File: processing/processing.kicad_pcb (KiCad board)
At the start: 2 copper layers, 26 parts, among them J1 HRO-TYPE-C-31-M-12, J2 Conn_01x03, J3 ICSP, SW1 SW_RESET, U1 CH340G, U2 ATmega328P-AU, Y1 12MHz, Y2 16MHz

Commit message: base audio board
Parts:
- R3, R4: footprint Resistor_SMD:R_1206_3216Metric -> Resistor_SMD:R_0603_1608Metric
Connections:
- J1 pad B4: Net-(F1-Pad2) -> (no net)
- J1 pad B9: Net-(F1-Pad2) -> (no net)

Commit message: finish the processing board
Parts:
- added J3: Conn_01x05, Connector_PinSocket_2.54mm:PinSocket_1x05_P2.54mm_Vertical, F.Cu at (155.4, 76.5)
- added J4: HRO-TYPE-C-31-M-12, Connector_USB:USB_C_Receptacle_HRO_TYPE-C-31-M-12, F.Cu at (150.3, 119.5)
- J1: value HRO-TYPE-C-31-M-12 -> Conn_01x02; footprint Connector_USB:USB_C_Receptacle_HRO_TYPE-C-31-M-12 -> Connector_PinSocket_2.54mm:PinSocket_1x02_P2.54mm_Vertical
- J2: footprint Connector_PinHeader_2.54mm:PinHeader_1x03_P2.54mm_Vertical -> Connector_PinSocket_2.54mm:PinSocket_1x03_P2.54mm_Vertical
- moved C10 32.1 mm to (137.3, 96.0), turned to 270 degrees
- moved J1 30.6 mm to (130.3, 97.8), turned to 180 degrees
- moved C9 29.7 mm to (137.8, 93.5)
- moved C8 29.4 mm to (140.8, 93.5), turned to 180 degrees
- moved L1 28.4 mm to (153.1, 106.5), turned to 270 degrees
- moved C4 28.2 mm to (164.1, 101.2), turned to 180 degrees
- moved Y2 26.2 mm to (140.3, 96.3), turned to 180 degrees
- moved R5 26.0 mm to (143.3, 96.5)
- moved U2 25.2 mm to (150.3, 96.5), turned to 315 degrees
- moved C6 23.8 mm to (155.1, 106.7), turned to 270 degrees
- moved U1 21.4 mm to (164.1, 107.3), turned to 0 degrees
- moved C7 21.2 mm to (153.2, 103.8)
- moved J5 20.1 mm to (138.8, 110.8), turned to 180 degrees
- moved SW1 19.7 mm to (162.1, 83.8), turned to 180 degrees
- moved C2 18.6 mm to (157.8, 107.4)
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- renumbered J3 to J5
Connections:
- J2 pad 3: A3 -> A2
- R1 pad 1: Net-(J1-PadA5) -> Net-(J4-PadA5)
- R2 pad 2: Net-(J1-PadB5) -> Net-(J4-PadB5)
- U1 pad 5: Net-(J1-PadA6) -> Net-(J4-PadA6)
- U1 pad 6: Net-(J1-PadA7) -> Net-(J4-PadA7)
- U2 pad 1: Net-(U2-Pad1) -> D2
- U2 pad 10: Net-(U2-Pad10) -> D5
- U2 pad 2: Net-(U2-Pad2) -> D3
- U2 pad 32: Net-(U2-Pad32) -> D1
- U2 pad 9: Net-(U2-Pad9) -> D4
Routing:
- net +5V: track 17.5 -> 106.7 mm, vias 0 -> 8
- net RESET: track 0.00 -> 43.4 mm, vias 0 -> 3
- net GND: track 44.9 -> 77.7 mm, vias 10 -> 9
- net D5: track 0.00 -> 26.4 mm, vias 0 -> 2
- net D4: track 0.00 -> 25.1 mm, vias 0 -> 2
- net RX: track 0.00 -> 20.9 mm, vias 0 -> 2
- net TX: track 0.00 -> 20.0 mm, vias 0 -> 2
- net Net-(J4-PadA7): track 0.00 -> 19.9 mm, vias 0 -> 2
- net Net-(J4-PadA6): track 0.00 -> 19.1 mm
- net D2: track 0.00 -> 17.4 mm
- net D3: track 0.00 -> 17.4 mm
- net A0: track 0.00 -> 17.0 mm
- net D1: track 0.00 -> 16.7 mm
- net A1: track 0.00 -> 16.4 mm
- net SCK: track 0.00 -> 15.8 mm, vias 0 -> 1
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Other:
- board outline added: 52 x 52 mm
- board text added: "RESET"

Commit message: fix design rules
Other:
- rule trace_min: 0.2 -> 0.127
- rule via_min_size: 0.4 -> 0.6

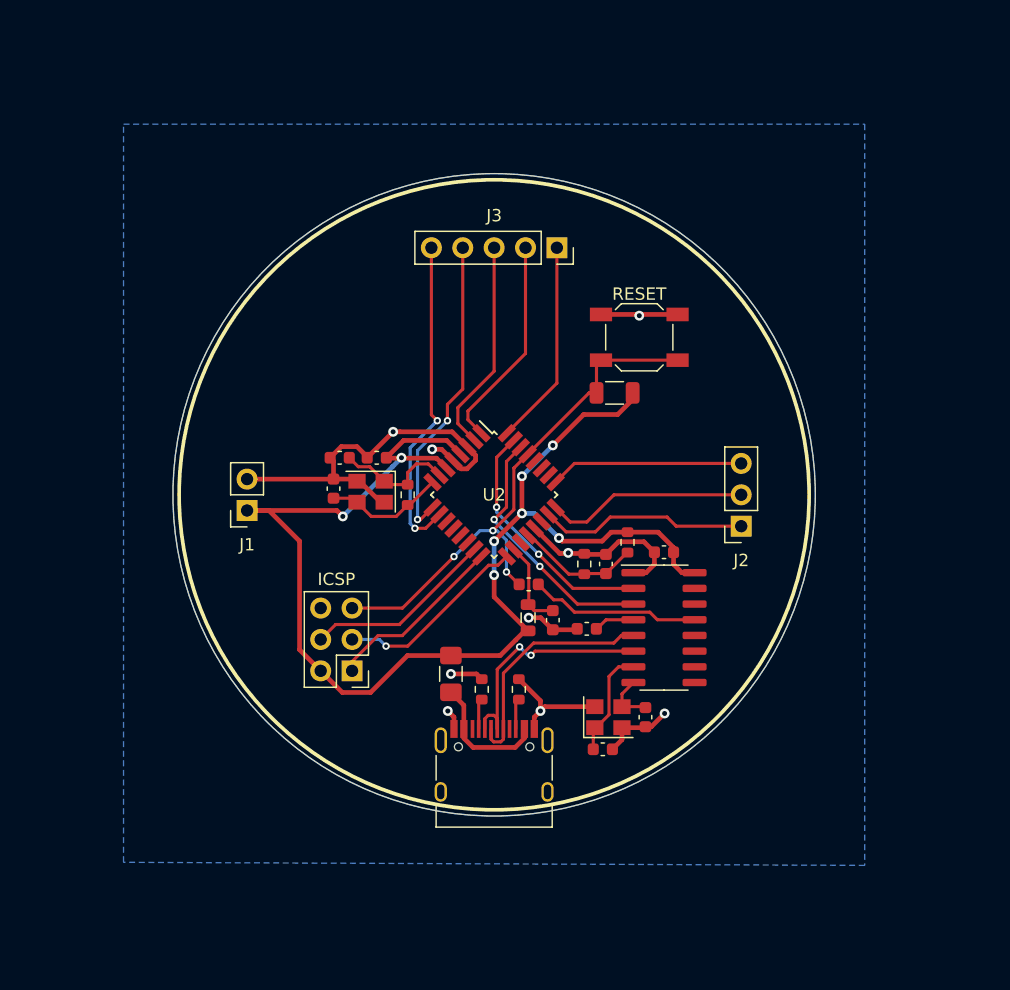
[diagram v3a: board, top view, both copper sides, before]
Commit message: resize boards
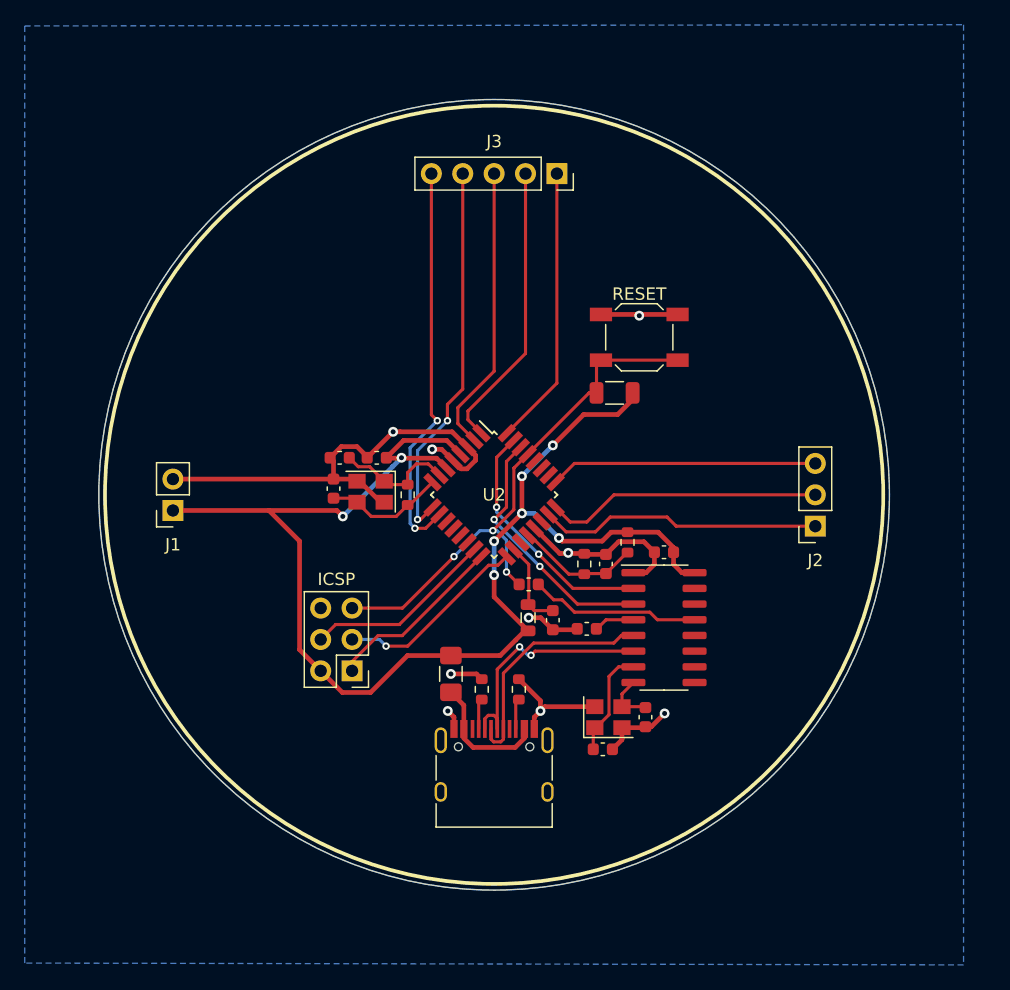
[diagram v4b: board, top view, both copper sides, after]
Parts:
- moved J1 6.00 mm to (124.3, 97.8)
- moved J2 6.00 mm to (176.3, 99.1)
- moved J3 6.00 mm to (155.4, 70.5)
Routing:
- net GND: track 77.7 -> 83.7 mm
- net D3: track 17.4 -> 23.4 mm
- net D5: track 26.4 -> 32.4 mm
- net D4: track 25.1 -> 31.1 mm
- net D2: track 17.4 -> 23.4 mm
- net D1: track 16.7 -> 22.7 mm
- net A2: track 15.6 -> 21.6 mm
- net A1: track 16.4 -> 22.4 mm
- net A0: track 17.0 -> 23.0 mm
- net +5V: track 106.7 -> 111.0 mm
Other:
- board size 52 x 52 mm -> 64 x 64 mm
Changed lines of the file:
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@@
   )
   (module Connector_PinSocket_2.54mm:PinSocket_1x02_P2.54mm_Vertical locked (layer F.Cu)
-    (at 130.35 97.82 180)
+    (at 124.35 97.82 180)
     (descr "Through hole straight socket strip, 1x02, 2.54mm pitch, single row (from Kicad 4.0.7), script generated")
     (tags "Through hole socket strip THT 1x02 2.54mm single row")
@@
   )
   (module Connector_PinSocket_2.54mm:PinSocket_1x05_P2.54mm_Vertical locked (layer F.Cu)
-    (at 155.43 76.55 270)
+    (at 155.43 70.55 270)
     (descr "Through hole straight socket strip, 1x05, 2.54mm pitch, single row (from Kicad 4.0.7), script generated")
     (tags "Through hole socket strip THT 1x05 2.54mm single row")
@@
   )
   (module Connector_PinSocket_2.54mm:PinSocket_1x03_P2.54mm_Vertical locked (layer F.Cu)
-    (at 170.35 99.09 180)
+    (at 176.35 99.09 180)
     (descr "Through hole straight socket strip, 1x03, 2.54mm pitch, single row (from Kicad 4.0.7), script generated")
     (tags "Through hole socket strip THT 1x03 2.54mm single row")
@@
     )
   )
+  (gr_circle (center 150.35 96.55) (end 182.35 96.55) (layer Edge.Cuts) (width 0.05))
+  (gr_circle (center 150.35 96.55) (end 181.85 96.55) (layer F.SilkS) (width 0.3))
+  (gr_circle (center 150.35 96.55) (end 182.35 96.55) (layer B.Cu) (width 0.01))
   (gr_text RESET (at 162.1 80.3) (layer F.SilkS)
     (effects (font (size 1 1) (thickness 0.15)))
   )
-  (gr_circle (center 150.35 96.55) (end 175.85 96.55) (layer F.SilkS) (width 0.3))
-  (gr_circle (center 150.35 96.55) (end 124.35 96.55) (layer B.Cu) (width 0.01))
-  (gr_circle (center 150.35 96.55) (end 124.35 96.55) (layer Edge.Cuts) (width 0.05))
   (via (at 146.6 114.05) (size 0.8) (drill 0.4) (layers F.Cu B.Cu) (net 1))
   (segment (start 147.1 114.55) (end 146.6 114.05) (width 0.381) (layer F.Cu) (net 1))
@@
   (segment (start 137.35 93.825) (end 137.075 93.55) (width 0.381) (layer F.Cu) (net 1))
   (segment (start 137.35 95.275) (end 137.35 93.825) (width 0.381) (layer F.Cu) (net 1))
-  (segment (start 137.345 95.28) (end 137.35 95.275) (width 0.381) (layer F.Cu) (net 1))
-  (segment (start 130.35 95.28) (end 137.345 95.28) (width 0.381) (layer F.Cu) (net 1))
   (segment (start 141.164249 97.15) (end 141.45 97.15) (width 0.381) (layer F.Cu) (net 1))
   (segment (start 139.464249 95.45) (end 141.164249 97.15) (width 0.381) (layer F.Cu) (net 1))
@@
   (segment (start 157 107.475) (end 157.075 107.4) (width 0.381) (layer F.Cu) (net 1))
   (segment (start 155.1 107.475) (end 157 107.475) (width 0.381) (layer F.Cu) (net 1))
+  (segment (start 137.345 95.28) (end 137.35 95.275) (width 0.381) (layer F.Cu) (net 1))
+  (segment (start 124.355 95.275) (end 124.35 95.28) (width 0.381) (layer F.Cu) (net 1))
+  (segment (start 137.35 95.275) (end 124.355 95.275) (width 0.381) (layer F.Cu) (net 1))
   (segment (start 160.425 110.475) (end 161.625 110.475) (width 0.254) (layer F.Cu) (net 2))
   (segment (start 159.65 111.25) (end 160.425 110.475) (width 0.254) (layer F.Cu) (net 2))
@@
   (segment (start 152.1 108.3) (end 152.7875 107.6125) (width 0.381) (layer F.Cu) (net 5))
   (via (at 138.099996 98.3) (size 0.8) (drill 0.4) (layers F.Cu B.Cu) (net 5))
-  (segment (start 130.35 97.82) (end 137.619996 97.82) (width 0.381) (layer F.Cu) (net 5))
   (segment (start 137.619996 97.82) (end 138.099996 98.3) (width 0.381) (layer F.Cu) (net 5))
   (segment (start 138.099996 98.3) (end 142.149998 94.249998) (width 0.381) (layer B.Cu) (net 5))
@@
   (segment (start 134.6 100.3) (end 134.6 109.09) (width 0.381) (layer F.Cu) (net 5))
   (segment (start 132.12 97.82) (end 134.6 100.3) (width 0.381) (layer F.Cu) (net 5))
-  (segment (start 130.35 97.82) (end 132.12 97.82) (width 0.381) (layer F.Cu) (net 5))
   (via (at 142.85 93.55) (size 0.8) (drill 0.4) (layers F.Cu B.Cu) (net 5))
   (segment (start 142.814988 93.585012) (end 142.85 93.55) (width 0.381) (layer F.Cu) (net 5))
@@
   (segment (start 155.85 100.3) (end 159.1 100.3) (width 0.381) (layer F.Cu) (net 5))
   (segment (start 155.6 100.05) (end 155.85 100.3) (width 0.381) (layer F.Cu) (net 5))
+  (segment (start 137.619996 97.82) (end 124.35 97.82) (width 0.381) (layer F.Cu) (net 5))
   (segment (start 161.1 101.225) (end 159.4 102.925) (width 0.254) (layer F.Cu) (net 6))
   (segment (start 161.15 101.225) (end 161.1 101.225) (width 0.254) (layer F.Cu) (net 6))
@@
   (segment (start 156.509798 98.75) (end 157.85 98.75) (width 0.254) (layer F.Cu) (net 13))
   (segment (start 157.85 98.75) (end 160.05 96.55) (width 0.254) (layer F.Cu) (net 13))
-  (segment (start 160.05 96.55) (end 170.35 96.55) (width 0.254) (layer F.Cu) (net 13))
-  (segment (start 170.35 99.09) (end 165.09 99.09) (width 0.254) (layer F.Cu) (net 14))
+  (segment (start 160.05 96.55) (end 176.35 96.55) (width 0.254) (layer F.Cu) (net 13))
   (segment (start 165.09 99.09) (end 164.35 98.35) (width 0.254) (layer F.Cu) (net 14))
   (segment (start 164.35 98.35) (end 159.75 98.35) (width 0.254) (layer F.Cu) (net 14))
@@
   (segment (start 158.55 99.55) (end 156.178427 99.55) (width 0.254) (layer F.Cu) (net 14))
   (segment (start 156.178427 99.55) (end 154.769417 98.14099) (width 0.254) (layer F.Cu) (net 14))
+  (segment (start 165.09 99.09) (end 176.35 99.09) (width 0.254) (layer F.Cu) (net 14))
   (segment (start 137.52 107.05) (end 136.31 108.26) (width 0.254) (layer F.Cu) (net 15))
   (segment (start 142.678427 107.05) (end 137.52 107.05) (width 0.254) (layer F.Cu) (net 15))
@@
   (via (at 150.55 97.55) (size 0.6) (drill 0.3) (layers F.Cu B.Cu) (net 25))
   (segment (start 156.849798 94.01) (end 155.335103 95.524695) (width 0.254) (layer F.Cu) (net 29))
-  (segment (start 170.35 94.01) (end 156.849798 94.01) (width 0.254) (layer F.Cu) (net 29))
+  (segment (start 156.849798 94.01) (end 176.35 94.01) (width 0.254) (layer F.Cu) (net 29))
   (via (at 145.75 90.550004) (size 0.6) (drill 0.3) (layers F.Cu B.Cu) (net 36))
-  (segment (start 145.27 76.55) (end 145.27 90.070004) (width 0.254) (layer F.Cu) (net 36))
   (segment (start 145.27 90.070004) (end 145.75 90.550004) (width 0.254) (layer F.Cu) (net 36))
   (segment (start 143.550001 98.876709) (end 143.936646 99.263354) (width 0.254) (layer B.Cu) (net 36))
@@
   (segment (start 145.930583 98.14099) (end 144.808219 99.263354) (width 0.254) (layer F.Cu) (net 36))
   (segment (start 145.75 90.550004) (end 143.550001 92.750003) (width 0.254) (layer B.Cu) (net 36))
+  (segment (start 145.27 90.070004) (end 145.27 70.55) (width 0.254) (layer F.Cu) (net 36))
   (via (at 144.15 98.55) (size 0.6) (drill 0.3) (layers F.Cu B.Cu) (net 37))
   (segment (start 144.390202 98.55) (end 145.364897 97.575305) (width 0.254) (layer F.Cu) (net 37))
@@
   (segment (start 146.569705 89.230295) (end 146.569705 90.552815) (width 0.254) (layer F.Cu) (net 37))
   (segment (start 147.81 87.99) (end 146.569705 89.230295) (width 0.254) (layer F.Cu) (net 37))
-  (segment (start 147.81 76.55) (end 147.81 87.99) (width 0.254) (layer F.Cu) (net 37))
+  (segment (start 147.81 87.99) (end 147.81 70.55) (width 0.254) (layer F.Cu) (net 37))
   (segment (start 147.414214 90.785786) (end 147.414214 89.485786) (width 0.254) (layer F.Cu) (net 38))
-  (segment (start 150.35 86.55) (end 150.35 76.55) (width 0.254) (layer F.Cu) (net 38))
   (segment (start 148.75901 92.130583) (end 147.414214 90.785786) (width 0.254) (layer F.Cu) (net 38))
   (segment (start 147.414214 89.485786) (end 150.35 86.55) (width 0.254) (layer F.Cu) (net 38))
+  (segment (start 150.35 86.55) (end 150.35 70.55) (width 0.254) (layer F.Cu) (net 38))
   (segment (start 149.324695 91.564897) (end 148.229899 90.470101) (width 0.254) (layer F.Cu) (net 39))
-  (segment (start 152.89 85.11) (end 152.89 76.55) (width 0.254) (layer F.Cu) (net 39))
   (segment (start 148.229899 89.770101) (end 152.89 85.11) (width 0.254) (layer F.Cu) (net 39))
   (segment (start 148.229899 90.470101) (end 148.229899 89.770101) (width 0.254) (layer F.Cu) (net 39))
+  (segment (start 152.89 85.11) (end 152.89 70.55) (width 0.254) (layer F.Cu) (net 39))
   (segment (start 155.43 87.510202) (end 151.375305 91.564897) (width 0.254) (layer F.Cu) (net 40))
-  (segment (start 155.43 76.55) (end 155.43 87.510202) (width 0.254) (layer F.Cu) (net 40))
+  (segment (start 155.43 70.55) (end 155.43 87.510202) (width 0.254) (layer F.Cu) (net 40))
   (segment (start 149.1 113.375) (end 149.35 113.125) (width 0.254) (layer F.Cu) (net 42))
   (segment (start 149.1 115.505) (end 149.1 113.375) (width 0.254) (layer F.Cu) (net 42))
@@
     (polygon
       (pts
-        (xy 180.35 66.55) (xy 180.35 126.55) (xy 120.35 126.3) (xy 120.35 66.55)
+        (xy 188.35 58.495313) (xy 188.35 134.604688) (xy 112.35 134.45625) (xy 112.35 58.596875)
       )
     )

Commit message: panelized and ready for manufacturing
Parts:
- moved F1 5.75 mm to (146.8, 116.8)
- moved J4 5.75 mm to (150.3, 125.3)
- moved R1 5.75 mm to (149.3, 118.0)
- moved R2 5.75 mm to (152.3, 118.0)
- moved R6 4.81 mm to (164.3, 86.0)
- moved SW1 4.81 mm to (166.3, 81.5)
- moved J5 4.65 mm to (135.1, 113.5)
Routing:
- net +5V: track 111.0 -> 130.3 mm
- net RESET: track 43.4 -> 53.5 mm
- net Net-(J4-PadA7): track 19.9 -> 25.7 mm
- net Net-(J4-PadA6): track 19.1 -> 24.9 mm
- net MOSI: track 15.5 -> 20.4 mm
- net MISO: track 14.8 -> 19.6 mm
- net SCK: track 15.8 -> 20.6 mm
- net GND: track 83.7 -> 88.2 mm

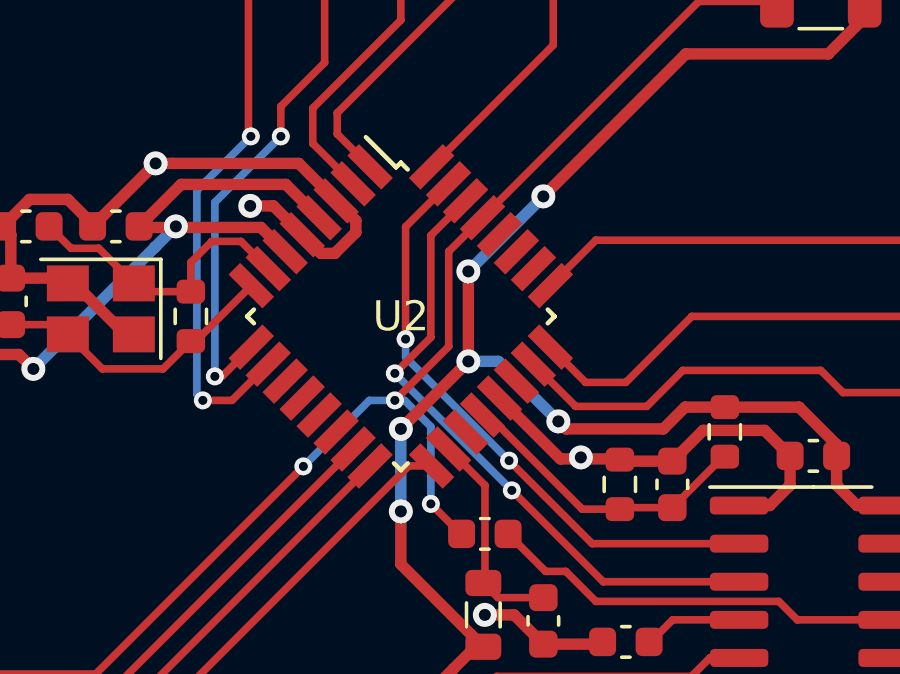
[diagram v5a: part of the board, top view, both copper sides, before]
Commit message: errata 1: rx and tx are flipped
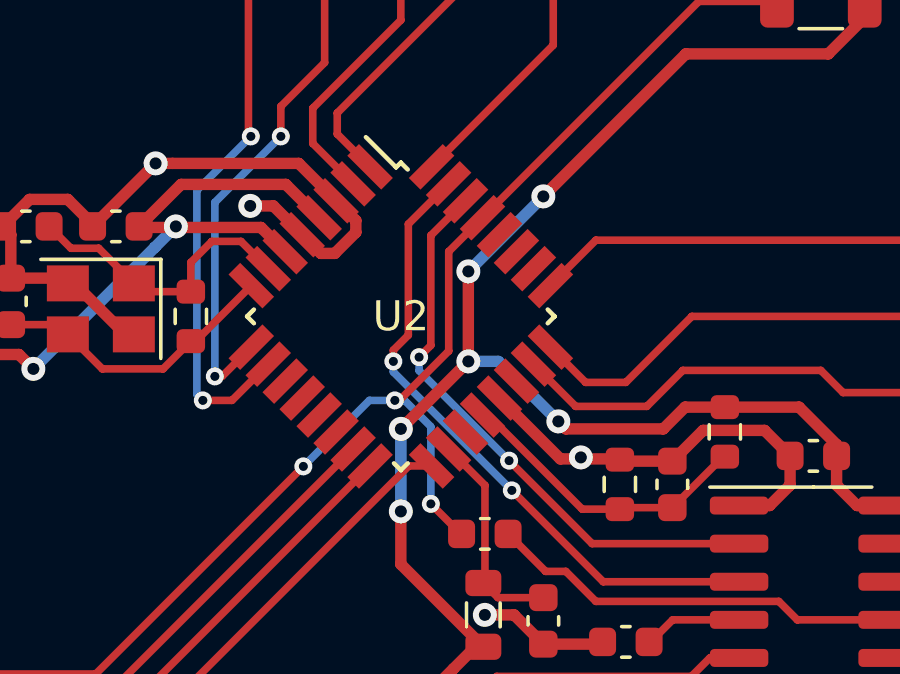
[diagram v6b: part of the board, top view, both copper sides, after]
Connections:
- U2 pad 30: RX -> TX
- U2 pad 31: TX -> RX
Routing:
- net TX: track 20.1 -> 19.4 mm
